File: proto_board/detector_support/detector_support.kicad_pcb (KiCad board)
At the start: 4 copper layers, 94 x 99.1 mm, 91 parts, among them J1 Programming Header, J10 Conn_01x06_Female, J11 DET_CONN, J2 DET_CONN_PWR, J3 BATT_1, J4 BATT_2, J5 BATT_3, J6 BATT_4, J7 TEST_CONN, J8 693072010801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

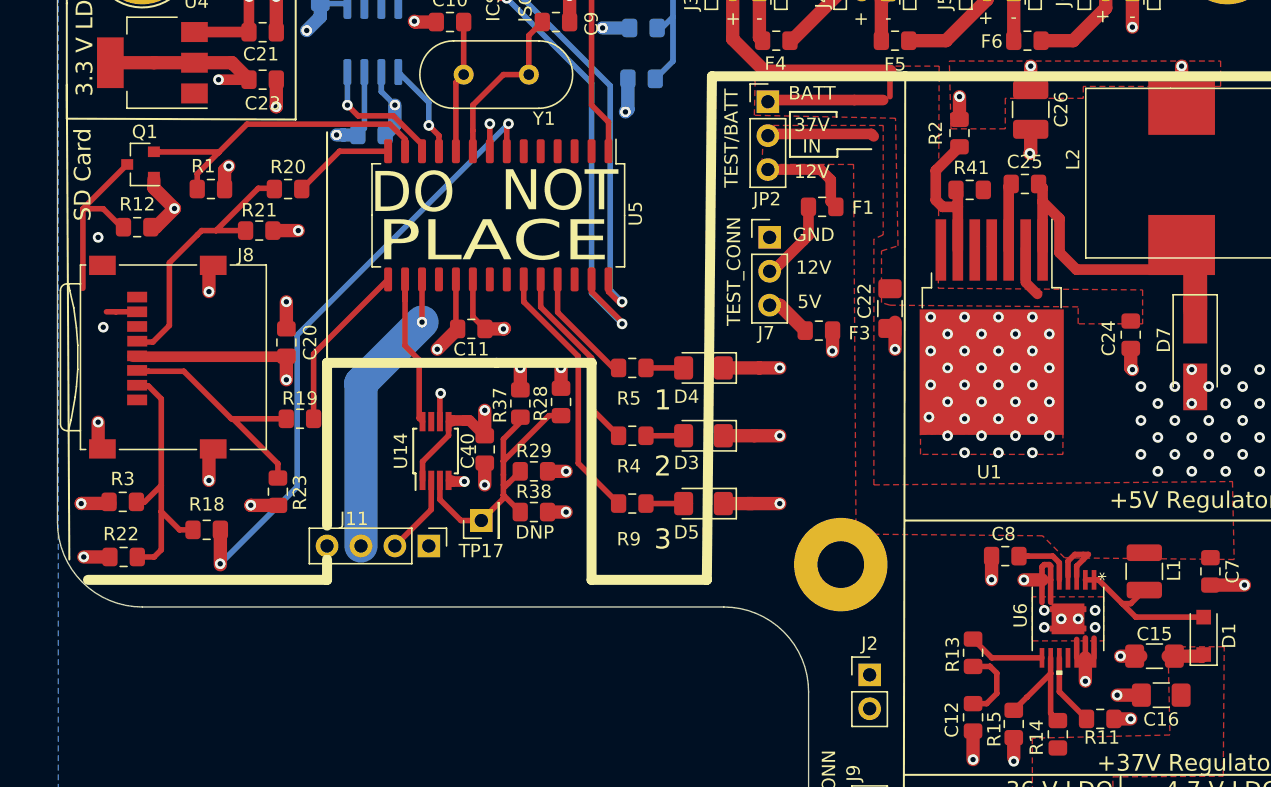
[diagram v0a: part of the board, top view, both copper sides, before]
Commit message: Removed unessary files, cleaned up repo put things in folders
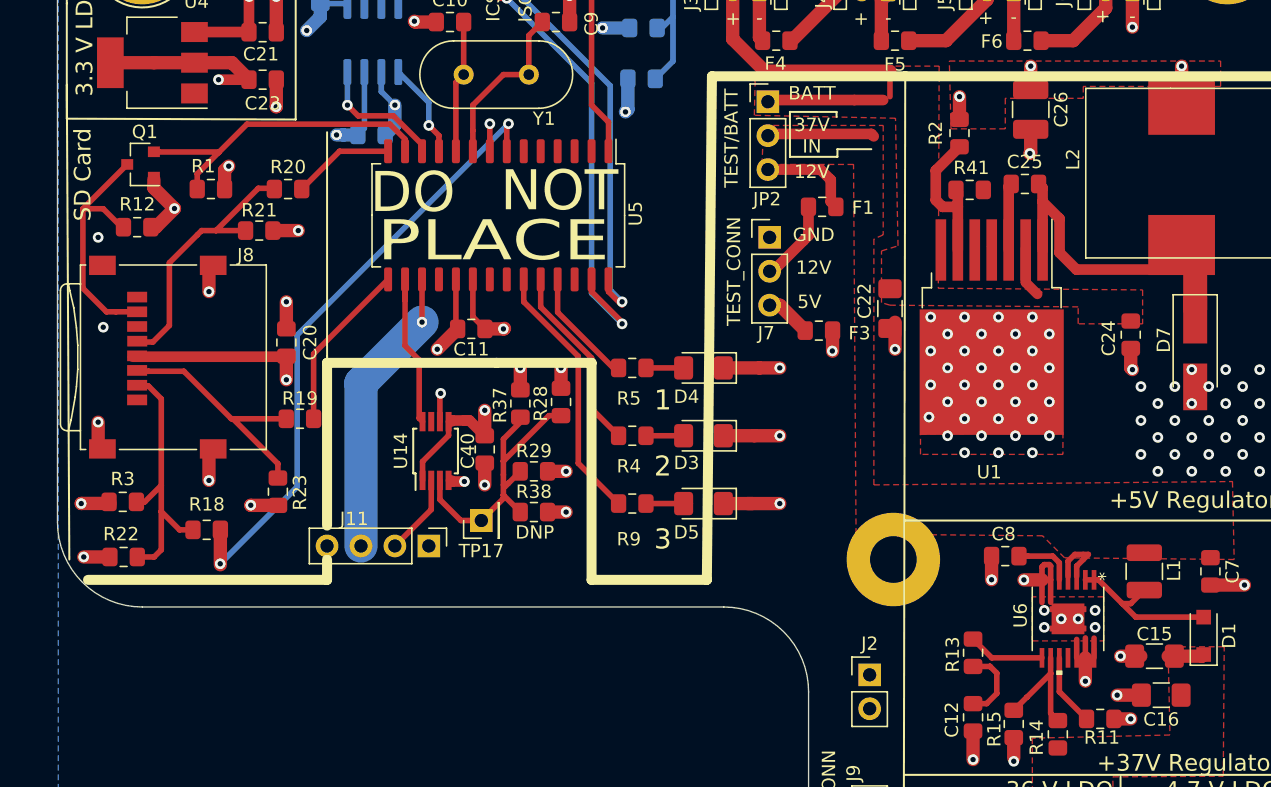
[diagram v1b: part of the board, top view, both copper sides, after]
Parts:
- moved REF** 3.96 mm to (146.4, 99.7)
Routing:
- net Net-(J8-Pad7): track 16.6 -> 19.0 mm

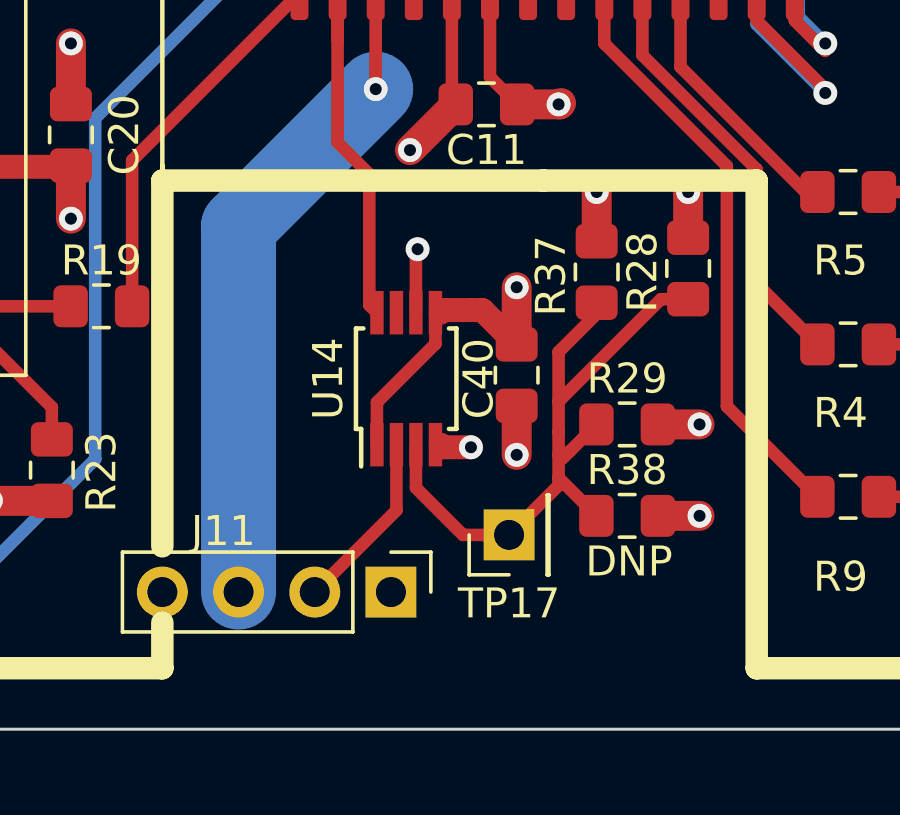
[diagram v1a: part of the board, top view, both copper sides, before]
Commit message: moved interfering test point and useless drill holes
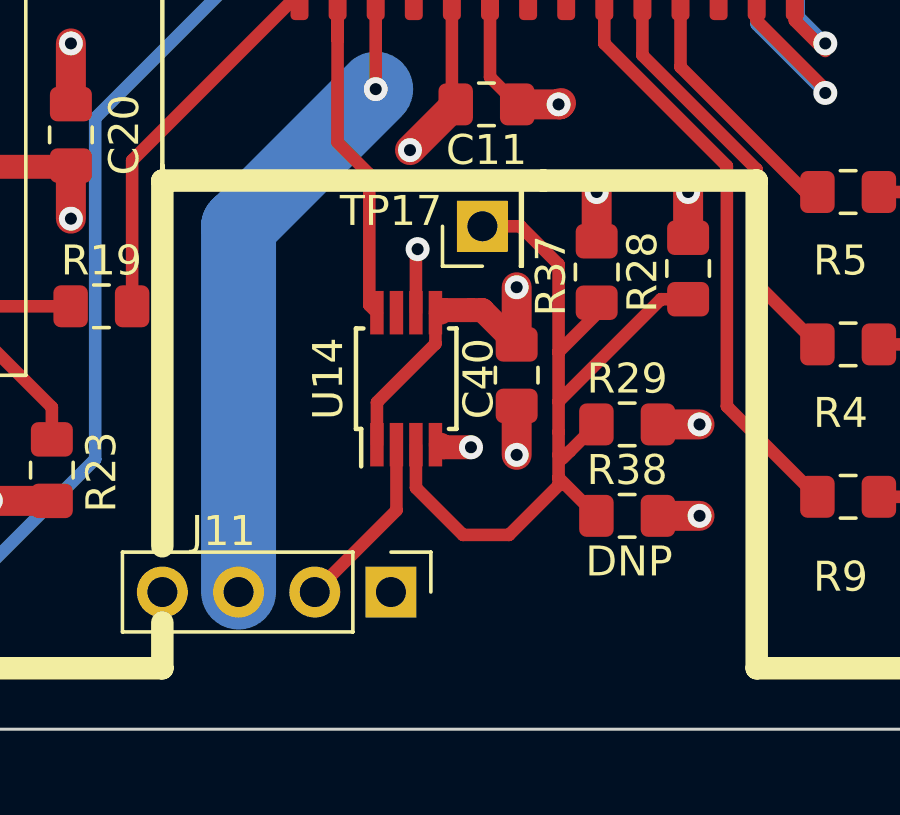
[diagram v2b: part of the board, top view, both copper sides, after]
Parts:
- moved TP17 10.3 mm to (114.7, 86.5)
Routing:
- net Net-(R28-Pad2): track 22.9 -> 28.8 mm

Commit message: Added volcano silkscreen, readme, and some connector lables i missed
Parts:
- added G***: LOGO, Payload2020_custom:volcano, B.Cu at (130.9, 97.7)

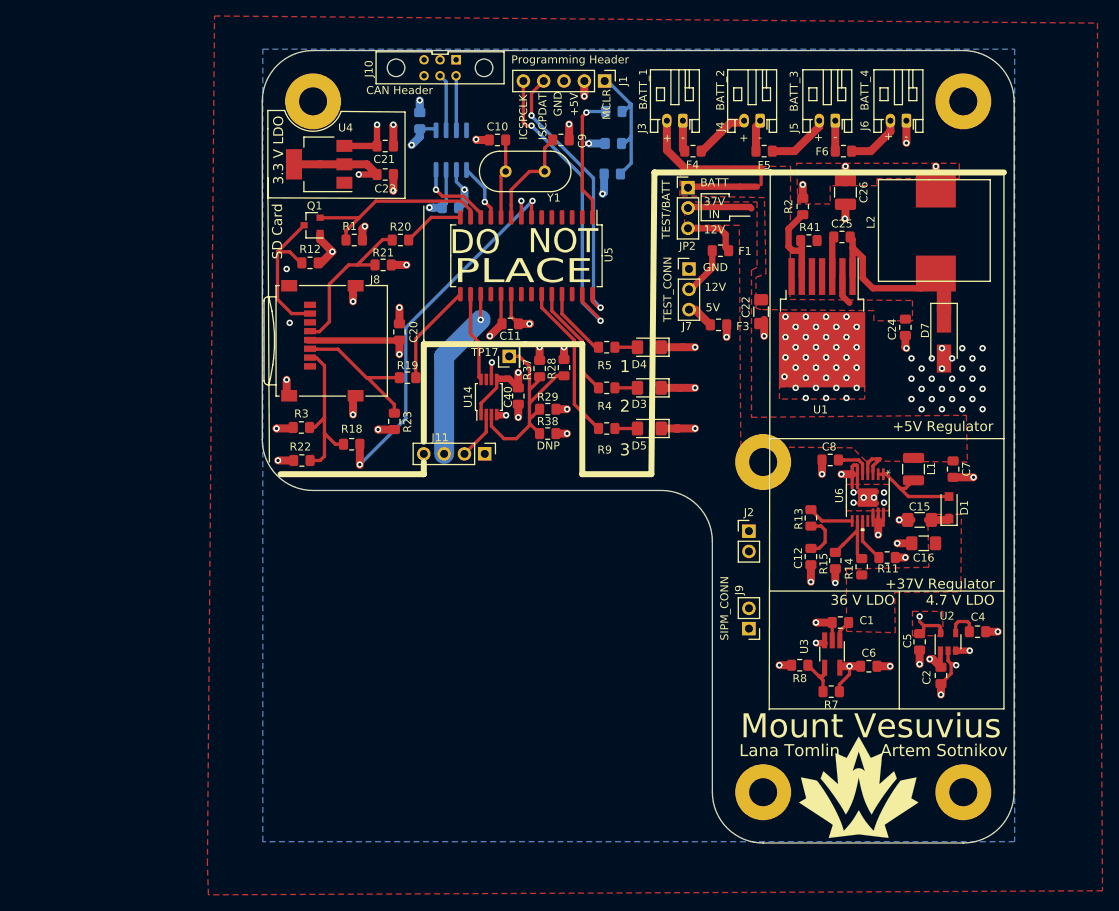
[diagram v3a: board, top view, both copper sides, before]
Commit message: Addressed Zachary's review, fixed some silkscreen issues and moved some components further apart. Added project information to README
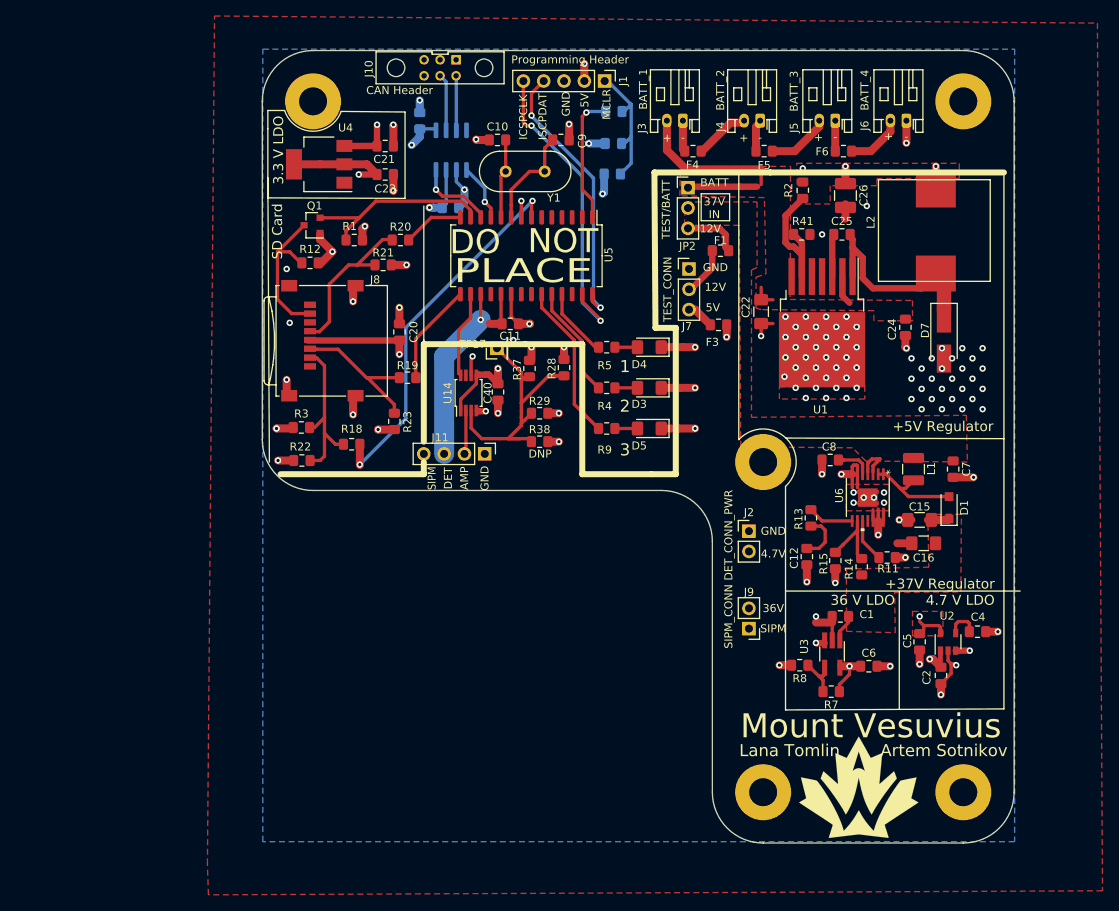
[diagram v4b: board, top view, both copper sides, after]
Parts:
- moved U14 2.59 mm to (109.6, 91.1)
- moved C40 2.59 mm to (113.3, 90.9)
- moved R2 2.03 mm to (151.4, 65.7)
- moved TP17 1.83 mm to (113.2, 85.5)
- moved R38 1.44 mm to (118.5, 97.2)
- moved R37 1.27 mm to (117.2, 88.0)
- moved R41 1.17 mm to (151.3, 71.2)
- moved R29 1.14 mm to (118.5, 93.6)
- moved C1 0.76 mm to (156.1, 119.0)
- moved C12 0.51 mm to (151.9, 111.5)
- moved C26 0.40 mm to (156.7, 66.4)
- moved C25 0.32 mm to (156.3, 71.2)
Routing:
- net Net-(C7-Pad1): track 12.9 -> 5.07 mm
- net Net-(R28-Pad2): track 28.8 -> 34.9 mm
- net Net-(R2-Pad2): track 11.5 -> 15.1 mm
- net +BATT: track 31.7 -> 34.7 mm
- net +5V: track 74.2 -> 72.5 mm
- net /INTERUPT_OUT: track 11.8 -> 10.9 mm
- net /AMP_OUT: track 6.04 -> 5.50 mm
- net Net-(C12-Pad1): track 5.61 -> 6.12 mm
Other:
- board text added: "36V"
- board text added: "4.7V"
- board text added: "AMP"
- board text added: "DET"
- board text added: "SIPM"
- board text removed: "+5V"

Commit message: Updataed gerbers
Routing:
- net +37V: track 5.39 -> 6.15 mm
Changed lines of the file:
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@@
     (thickness 1.6)
     (drawings 119)
-    (tracks 620)
+    (tracks 621)
     (zones 0)
     (modules 92)
@@
       (drillshape 0)
       (scaleselection 1)
-      (outputdirectory "GERBERS_/"))
+      (outputdirectory "GERBERS_support/"))
   )
   (net 0 "")
@@
   (segment (start 156.017 120.852) (end 157.108 119.761) (width 0.42) (layer Papa.Cu) (net 55))
   (segment (start 156.017 121.988) (end 156.017 120.852) (width 0.42) (layer Papa.Cu) (net 55))
+  (segment (start 157.108 119.761) (end 157.108 118.999) (width 0.42) (layer Papa.Cu) (net 55))
   (segment (start 165.989 119.634) (end 165.989 119.634) (width 0.8) (layer Papa.Cu) (net 56))
   (segment (start 168.595 121.074) (end 168.595 120.335) (width 0.42) (layer Papa.Cu) (net 56))

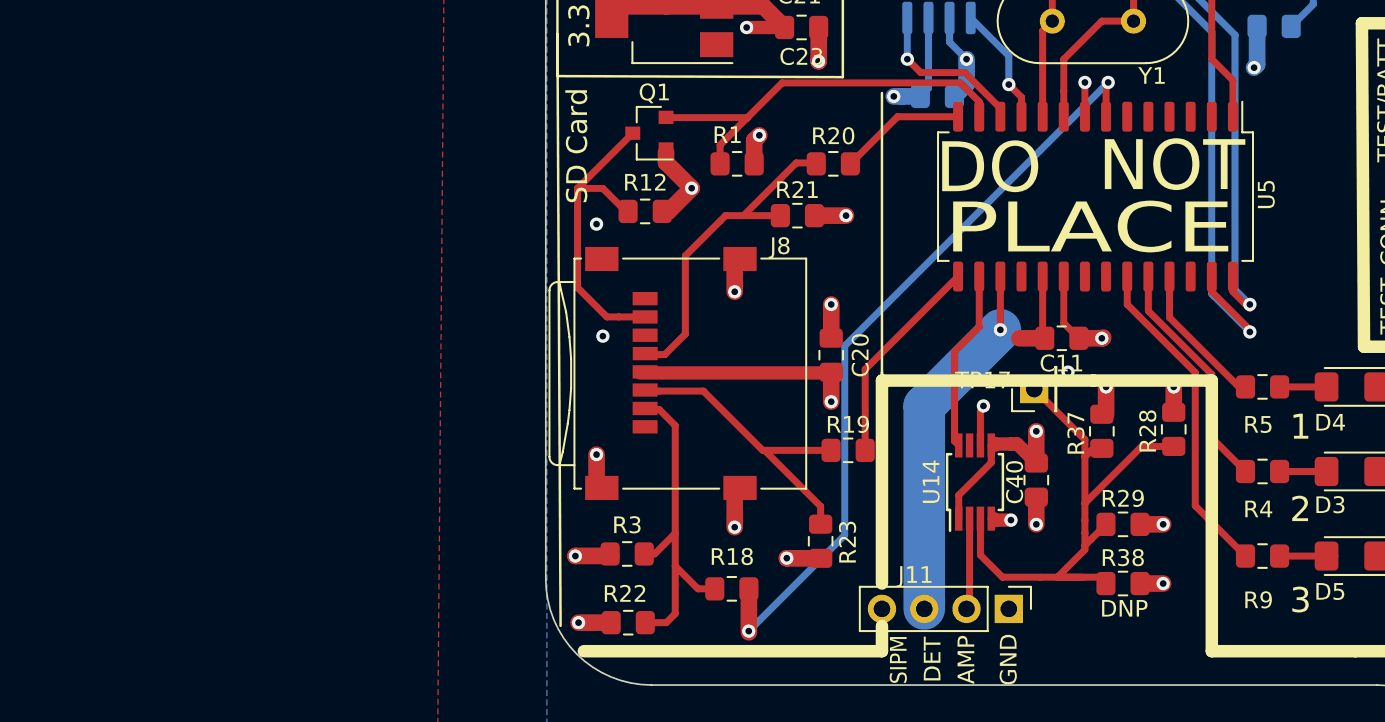
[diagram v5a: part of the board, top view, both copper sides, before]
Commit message: Fix up detector board issues
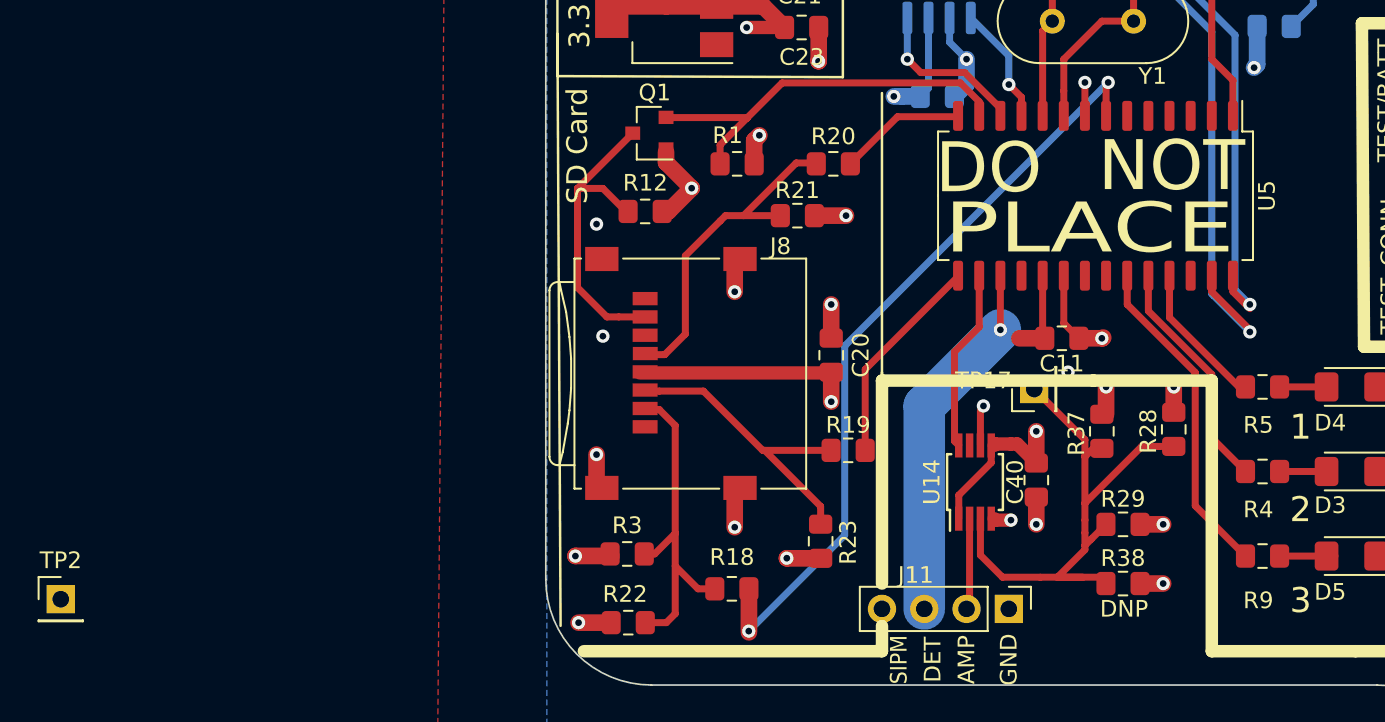
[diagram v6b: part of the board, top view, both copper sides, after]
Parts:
- added TP2: INTERRUPT, Connector_PinHeader_2.54mm:PinHeader_1x01_P2.54mm_Vertical, F.Cu at (54.7, 98.1)
- moved U5 0.05 mm to (116.8, 73.9)
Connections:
- J10 pad 1: (no net) -> Net-(J10-Pad1)
- J10 pad 2: (no net) -> Net-(J10-Pad2)
- J10 pad 6: (no net) -> Net-(J10-Pad6)
- J11 pad 4: /SIPM_OUT -> /SIPM_OUT_DET
- J8 pad 1: (no net) -> Net-(J8-Pad1)
- J8 pad 8: (no net) -> Net-(J8-Pad8)
- U1 pad 5: (no net) -> Net-(U1-Pad5)
- U1 pad 7: (no net) -> Net-(U1-Pad7)
- U14 pad 7: (no net) -> Net-(U14-Pad7)
- U5 pad 18: (no net) -> Net-(U5-Pad18)
- U5 pad 2: (no net) -> Net-(U5-Pad2)
- U5 pad 21: (no net) -> Net-(U5-Pad21)
- U5 pad 22: (no net) -> Net-(U5-Pad22)
- U5 pad 26: (no net) -> Net-(U5-Pad26)
- U5 pad 3: (no net) -> Net-(U5-Pad3)
- U5 pad 4: (no net) -> Net-(U5-Pad4)
- U5 pad 5: (no net) -> Net-(U5-Pad5)
- U5 pad 6: (no net) -> Net-(U5-Pad6)
- U6 pad 11: (no net) -> Net-(U6-Pad11)
